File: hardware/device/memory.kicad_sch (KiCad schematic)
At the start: 10 parts, among them IC1 W25Q512JVEIQ, IC2 IS42S16160J-7BLI, J3 MICRO_SD

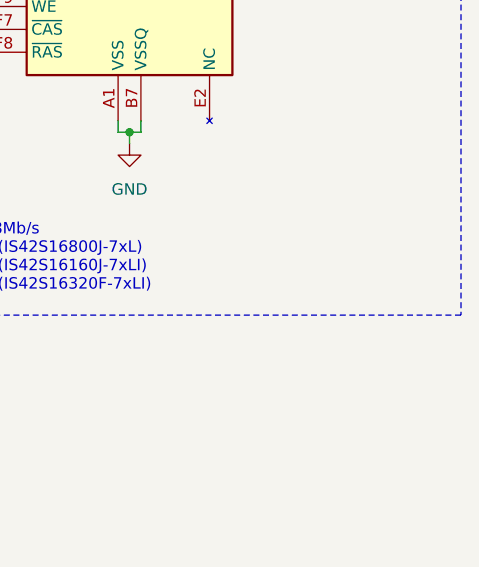
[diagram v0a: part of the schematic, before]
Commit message: feat: start adding battery fuel gauge
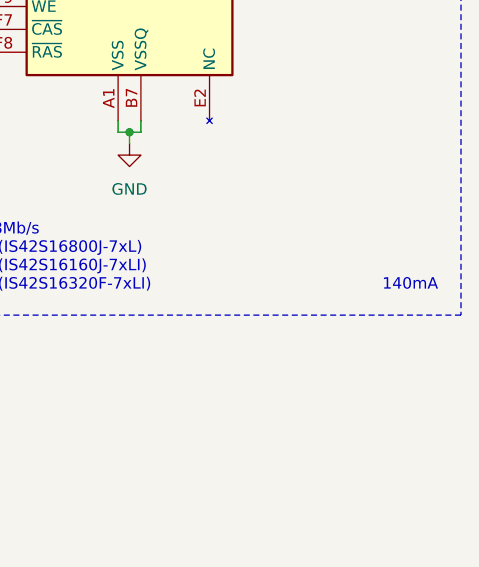
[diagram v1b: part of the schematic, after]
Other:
- note added: "140mA"
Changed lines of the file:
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@@
+		)
+	)
+	(text "140mA"
+		(exclude_from_sim no)
+		(at 262.89 138.43 0)
+		(effects
+			(font
+				(size 1.27 1.27)
+				(thickness 0.1588)
+				(color 132 132 132 1)
+			)
+			(justify right bottom)
 		)
 	)

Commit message: chore: schematic organization
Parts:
- IC1: JLC (none) -> C7389628
- IC2: JLC (none) -> C1348766
- J3: JLC (none) -> C114218
- R13, R14, R15, R16, R17: footprint (none) -> Resistor_SMD:R_0402_1005Metric
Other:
- note added: "Memory Storage Calculations: 16bit * 48000Hz = 768,000b/s = 0.768Mb/s 128Mb / 0.768Mb/s = 166.66 seconds (IS42S16800J-7xL) 256Mb / 0.768Mb/s = 333.33 seconds (IS42S16160J-7xLI) 512Mb / 0.768Mb/s = 666.66 seconds (IS42S16320F-7xLI)"
- note added: "Micro SD Card (Project and Sample Storage)"
- note added: "Operates in SPI mode as we don't need a particularly fast transfer speed. Most data that's stored/read from the card is loaded once and cached in SDRAM while the project is open."
- note added: "Project and sample storage"
- note added: "Project working memory"
- note added: "Recording and effects memory"
- note added: "The SDRAM is used as an cache for processing audio effects, such as reverb, delay, etc. and for live recording and editing before comitting to long-term memory (SD card)."
- note added: "The internal flash memory stores device settings and statistics, and loads and caches samples for the currently open project. Caching project samples allows for streaming the audio directly from the flash memory, vs trying to stream it from the slower SPI SD card. By caching the project in flash, it can also be loaded instantly when the device is turned on without waiting to load from the SD card."
- note removed: "140mA"
- note removed: "16bit * 48000Hz = 768,000b/s = 0.768Mb/s 128Mb / 0.768Mb/s = 166.66 seconds (IS42S16800J-7xL) 256Mb / 0.768Mb/s = 333.33 seconds (IS42S16160J-7xLI) 512Mb / 0.768Mb/s = 666.66 seconds (IS42S16320F-7xLI)"
- note removed: "Operates in SPI mode as we don't need a particularly fast transfer speed = most data that's stored/read from the card is loaded once and cached in SDRAM while the project is open."
- note removed: "Project and Sample Storage Micro SD Card"
- moved on the sheet: C21, C22, IC1, IC2, J3, R13, R14, R15, R16, R17

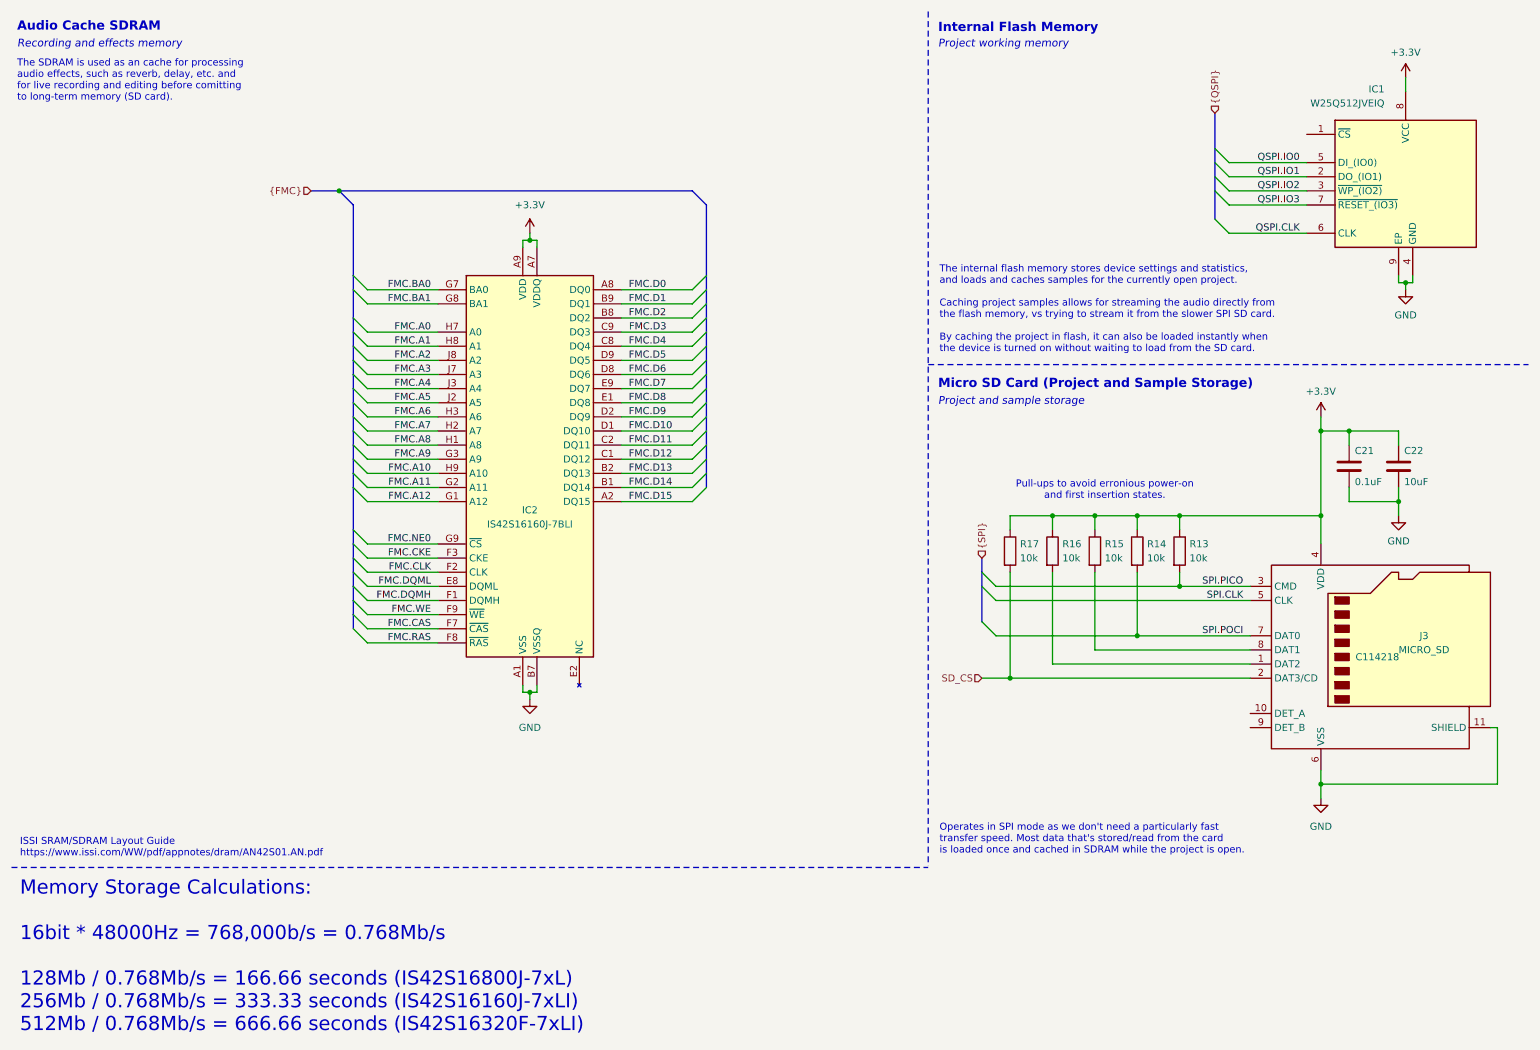
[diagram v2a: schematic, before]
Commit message: feat: add plated mounting holes
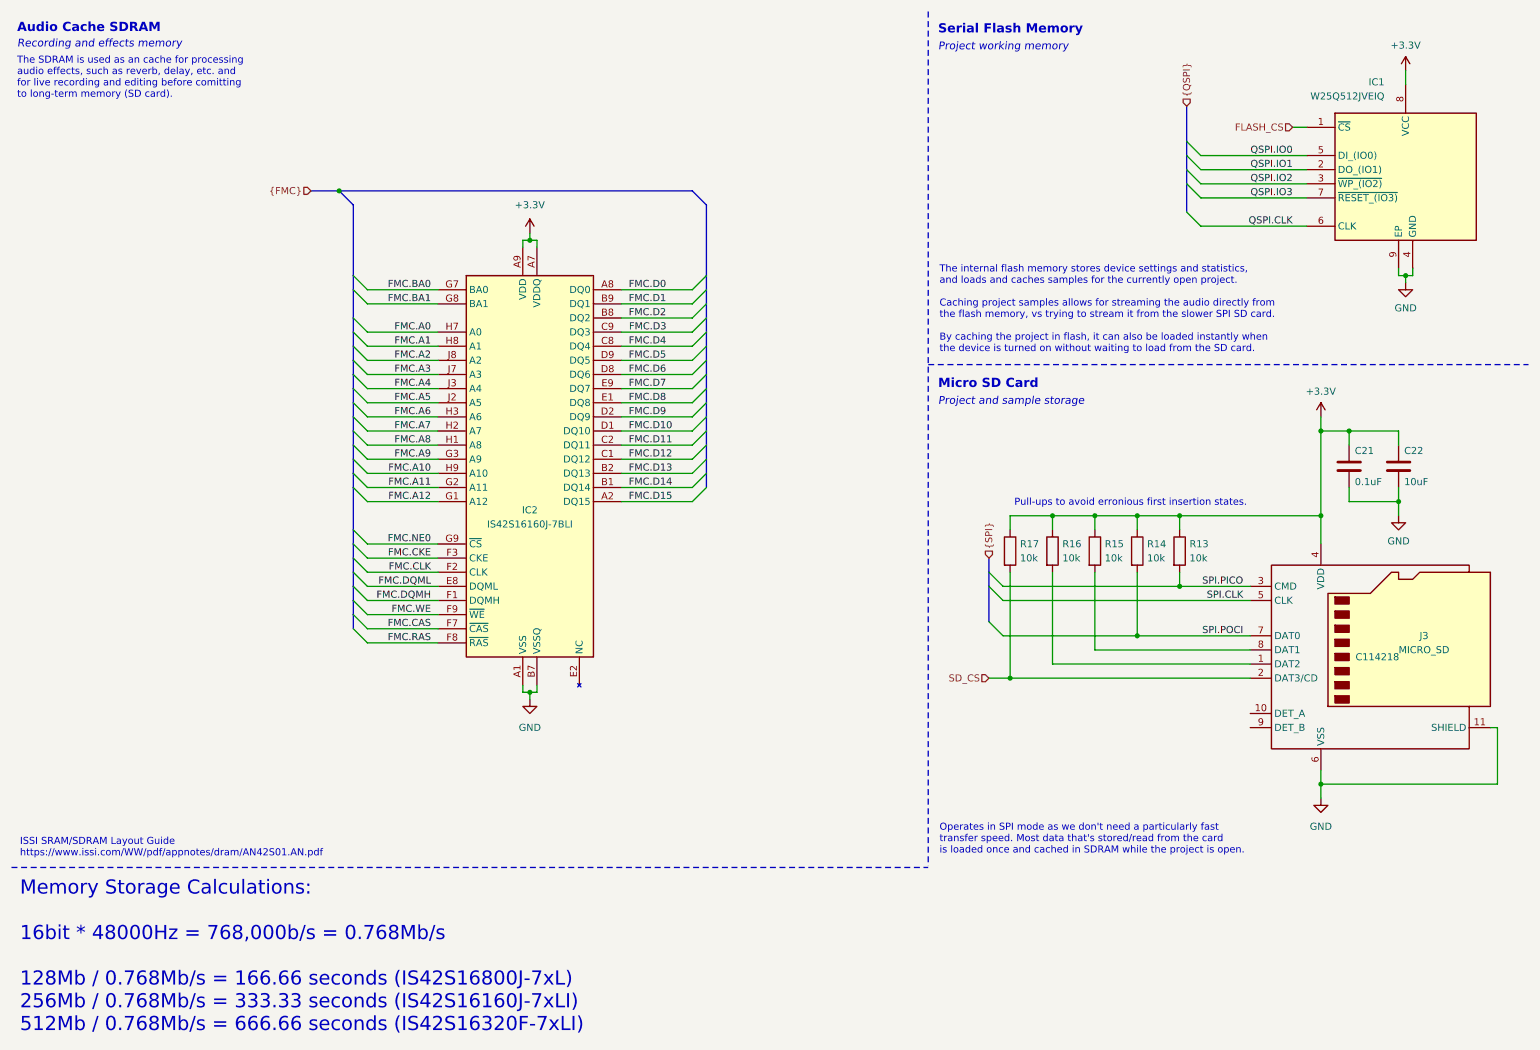
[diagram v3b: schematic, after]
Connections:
- net FLASH_CS: now reaches IC1.1 (~{CS})
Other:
- note added: "Micro SD Card"
- note added: "Pull-ups to avoid erronious first insertion states."
- note added: "Serial Flash Memory"
- note removed: "Internal Flash Memory"
- note removed: "Micro SD Card (Project and Sample Storage)"
- note removed: "Pull-ups to avoid erronious power-on and first insertion states."
- moved on the sheet: IC1

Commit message: feat: various routing, footprint and schematic cleanup
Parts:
- C21, C22: footprint Capacitor_SMD:C_0603_1608Metric_Pad1.08x0.95mm_HandSolder -> Capacitor_SMD:C_0402_1005Metric
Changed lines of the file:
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@@
 			)
 		)
-		(property "Footprint" "Capacitor_SMD:C_0603_1608Metric_Pad1.08x0.95mm_HandSolder"
+		(property "Footprint" "Capacitor_SMD:C_0402_1005Metric"
 			(at 253.6952 97.79 0)
 			(effects
@@
 			)
 		)
-		(property "Footprint" "Capacitor_SMD:C_0603_1608Metric_Pad1.08x0.95mm_HandSolder"
+		(property "Footprint" "Capacitor_SMD:C_0402_1005Metric"
 			(at 262.5852 97.79 0)
 			(effects

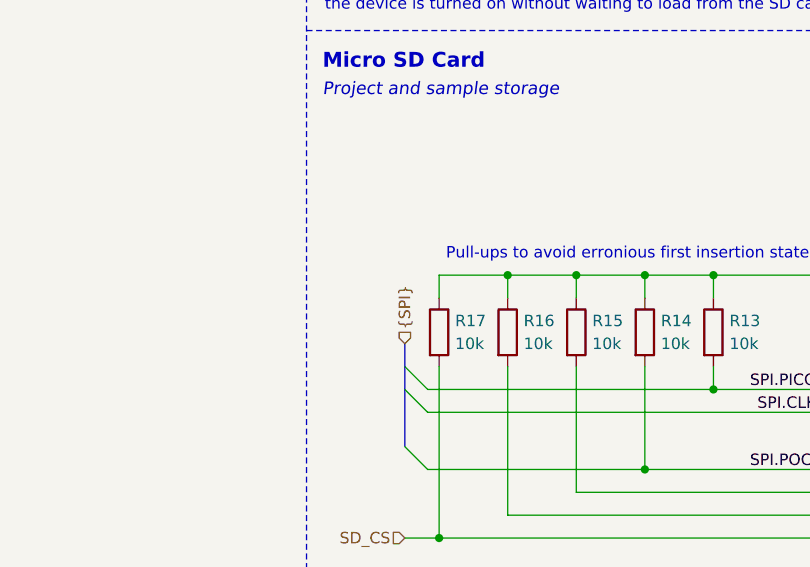
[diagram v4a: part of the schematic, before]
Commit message: feat: start replacing expansion  port with bluetooth module
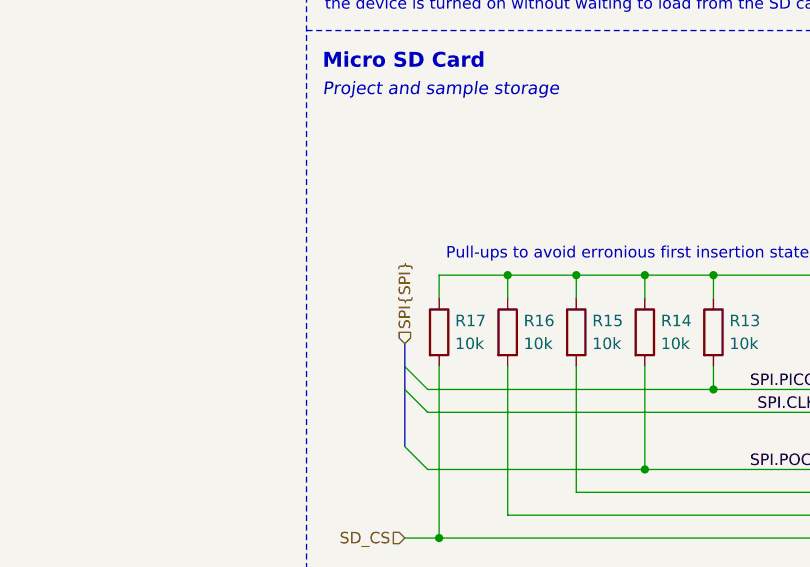
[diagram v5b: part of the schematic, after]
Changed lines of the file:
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@@
 		)
 	)
-	(hierarchical_label "{SPI}"
+	(hierarchical_label "SPI{SPI}"
 		(shape input)
 		(at 187.96 110.49 90)
